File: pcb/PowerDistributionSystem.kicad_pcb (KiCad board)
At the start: 4 copper layers, 60 x 59 mm, 92 parts, among them J1 Pin-Out, J2 JST-PH, J3 JST-PH, J4 JST-PH, J5 JST-PH, J6 JST-PH, U1 D24V7F5, U2 D24V7F3, U3 TMC2209-LA-T, U4 TMC2209-LA-T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

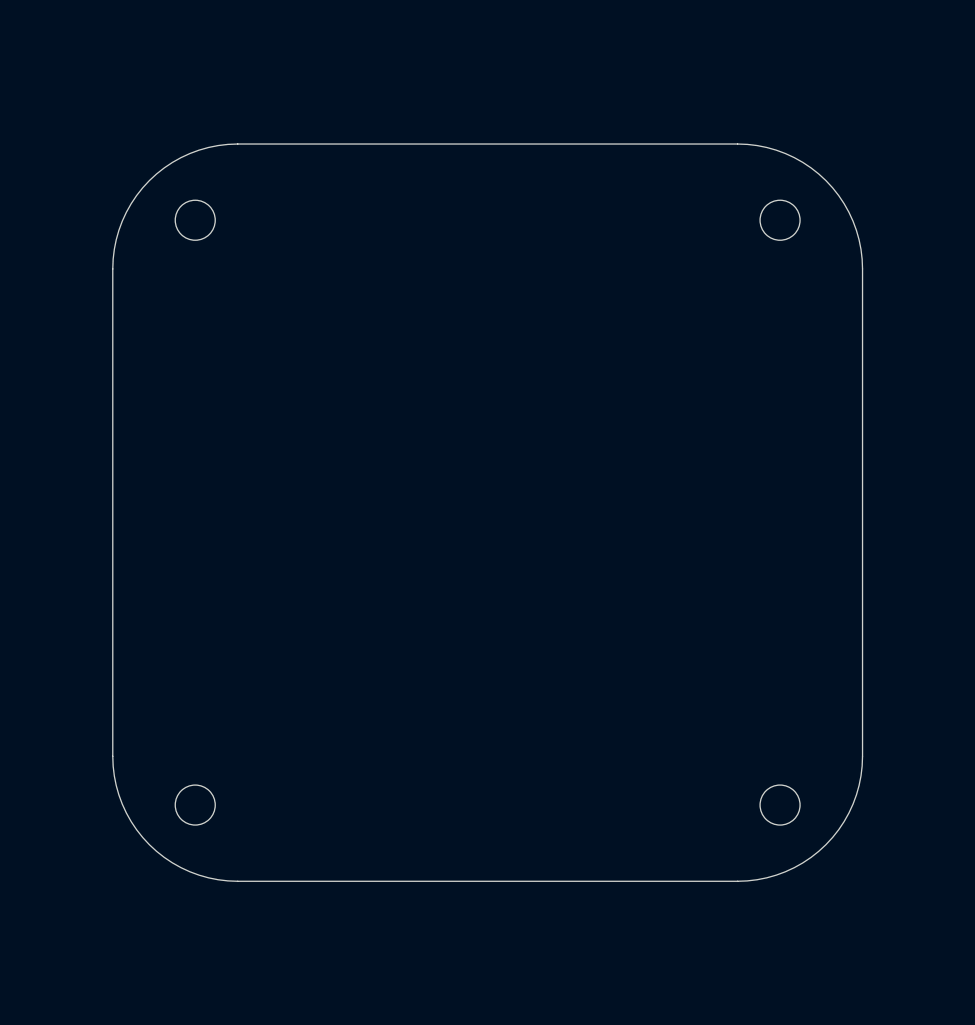
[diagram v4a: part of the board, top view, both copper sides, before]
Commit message: Using same layout as the main stack.
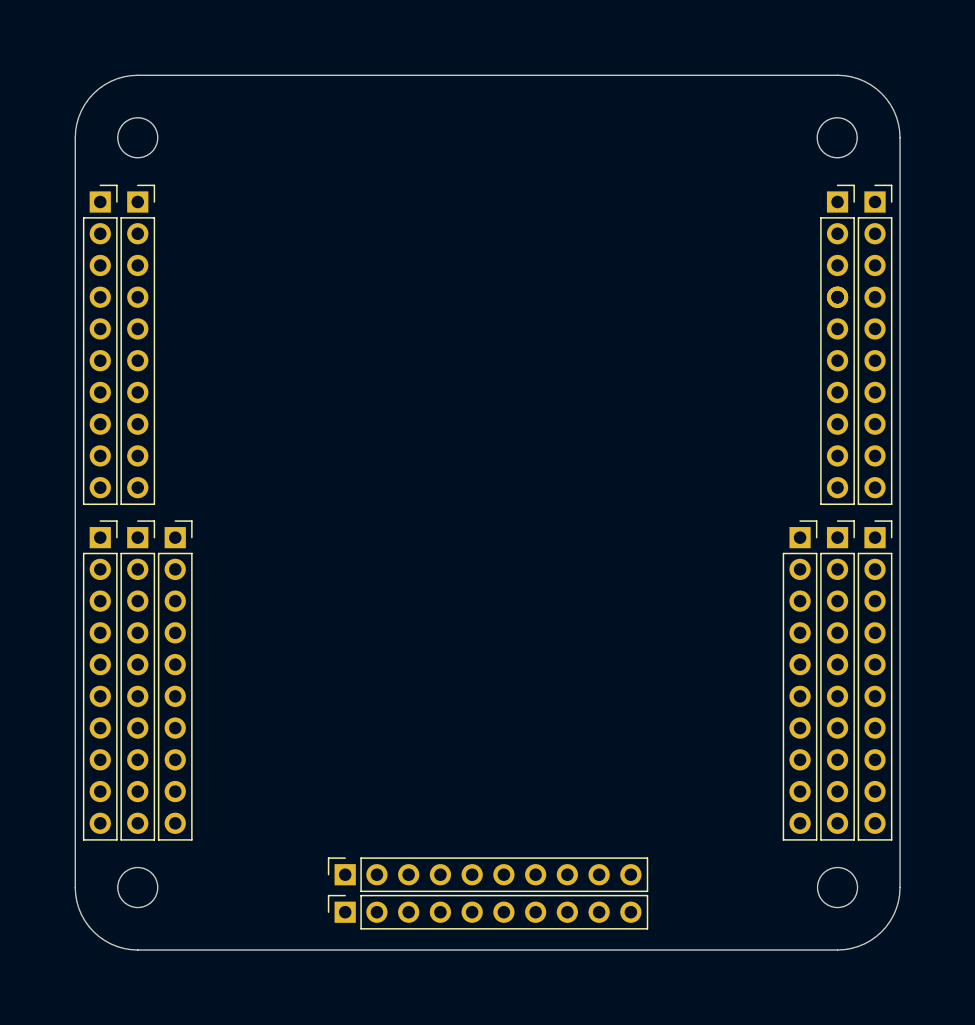
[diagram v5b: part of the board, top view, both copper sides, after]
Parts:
- removed H17, H18, H19, H20: MountingHole, MountingHole:MountingHole_3.2mm_M3
- added ?: , , F.Cu at (178.0, 82.8)
- added H1: M3, MountingHole:MountingHole_3.2mm_M3, F.Cu at (122.0, 130.0)
- added H2: M3, MountingHole:MountingHole_3.2mm_M3, F.Cu at (178.0, 70.0)
- added H3: M3, MountingHole:MountingHole_3.2mm_M3, F.Cu at (122.0, 70.0)
- added H4: M3, MountingHole:MountingHole_3.2mm_M3, F.Cu at (178.0, 130.0)
- added J11: Conn_01x10, pcb:Stack_Connector_1x10, F.Cu at (122.0, 75.1)
- added J12: Conn_01x10, pcb:Stack_Connector_1x10, F.Cu at (119.0, 102.0)
- added J13: Conn_01x10, pcb:Stack_Connector_1x10, F.Cu at (122.0, 102.0)
- added J14: Conn_01x10, pcb:Stack_Connector_1x10, F.Cu at (178.0, 75.1)
- added J15: Conn_01x10, pcb:Stack_Connector_1x10, F.Cu at (181.0, 75.1)
- added J16: Conn_01x10, pcb:Stack_Connector_1x10, F.Cu at (178.0, 102.0)
- added J17: Conn_01x10, pcb:Stack_Connector_1x10, F.Cu at (181.0, 102.0)
- added J18: Conn_01x10, pcb:Stack_Connector_1x10, F.Cu at (138.6, 129.0)
- added J19: Conn_01x10, pcb:Stack_Connector_1x10, F.Cu at (175.0, 102.0)
- added J21: Conn_01x10, pcb:Stack_Connector_1x10, F.Cu at (138.6, 132.0)
- added J23: Conn_01x10, pcb:Stack_Connector_1x10, F.Cu at (125.0, 102.0)
- added J3: Conn_01x10, pcb:Stack_Connector_1x10, F.Cu at (119.0, 75.1)
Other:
- board size 60 x 59 mm -> 66 x 70 mm

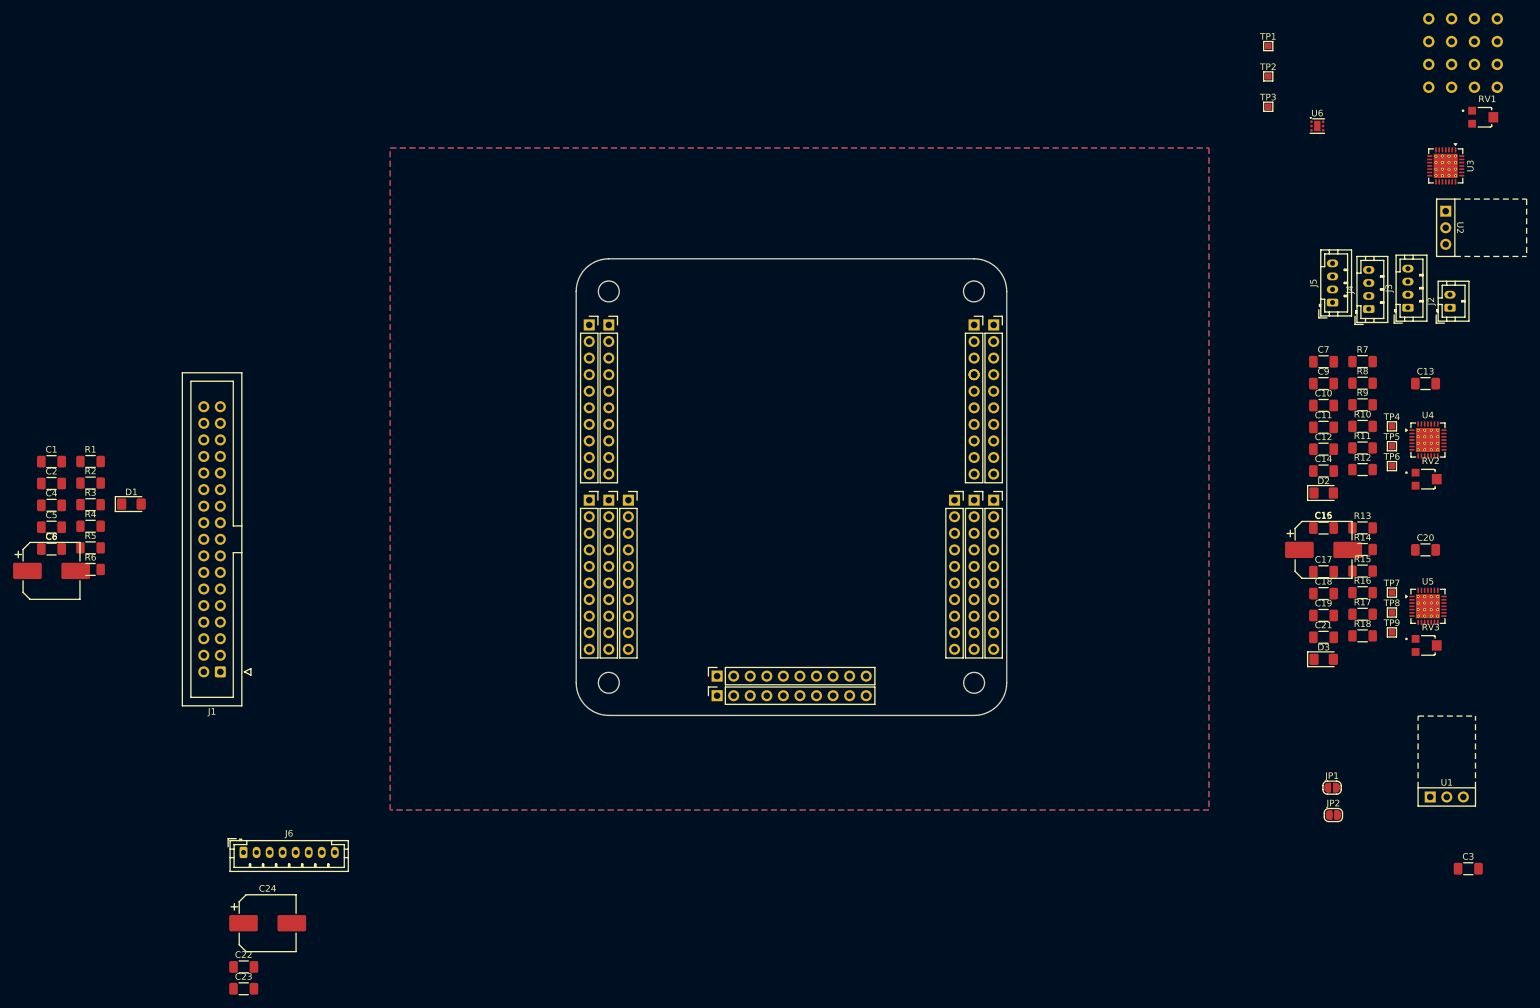
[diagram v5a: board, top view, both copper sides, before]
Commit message: Power distribution board using the PCB stack-up symbol.
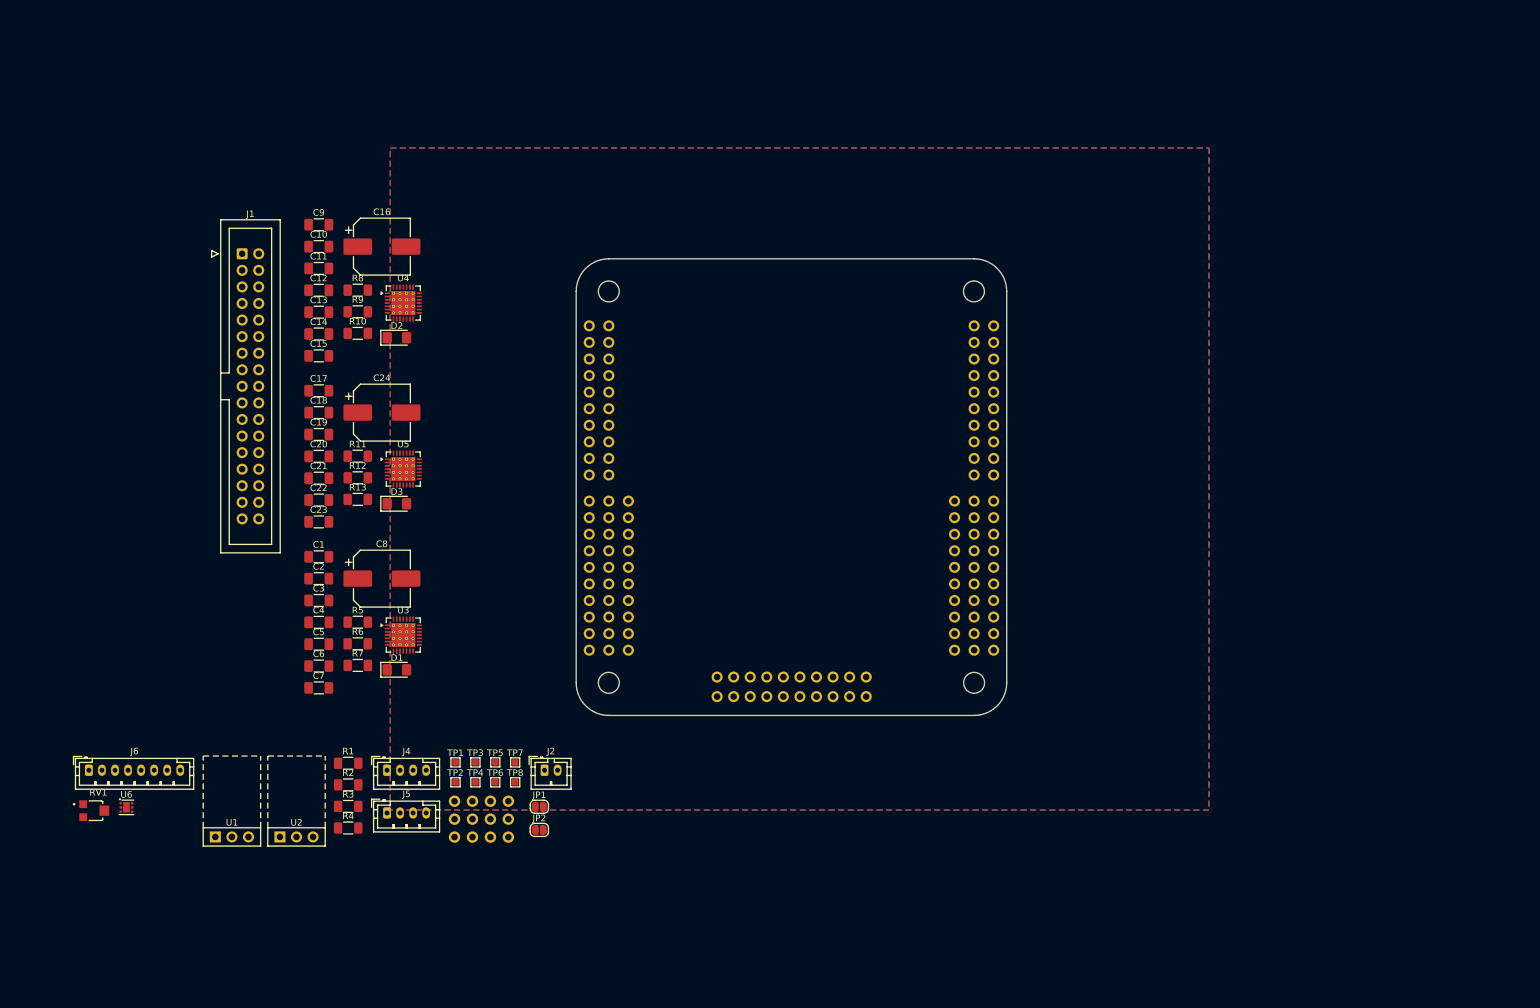
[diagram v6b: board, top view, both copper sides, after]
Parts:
- removed ?: , 
- removed H1, H2, H3, H4: M3, MountingHole:MountingHole_3.2mm_M3
- removed H1, H2, H3, H4: MountingHole_Pad_MP, pcb:Matrix_Hole
- removed J11, J12, J13, J14, J15, J16, J17, J18, J19, J21, J23, J3: Conn_01x10, pcb:Stack_Connector_1x10
- removed J3: JST-PH, Connector_JST:JST_PH_B4B-PH-K_1x04_P2.00mm_Vertical
- removed R14: 20k, Resistor_SMD:R_1206_3216Metric_Pad1.30x1.75mm_HandSolder
- removed R15: 1k, Resistor_SMD:R_1206_3216Metric_Pad1.30x1.75mm_HandSolder
- removed R16, R17: RL1206FR-070R05L, Resistor_SMD:R_1206_3216Metric_Pad1.30x1.75mm_HandSolder
- removed R18: 33k, Resistor_SMD:R_1206_3216Metric_Pad1.30x1.75mm_HandSolder
- removed RV2, RV3: 10k, pcb:TRIM_35WR10KLFTR
- removed TP9: TestPoint, TestPoint:TestPoint_Pad_1.0x1.0mm
- added C25: ~, pcb:StackConnector, F.Cu at (150.0, 100.0)
- moved RV1 238.0 mm to (43.0, 149.6)
- moved U6 210.3 mm to (48.0, 149.1)
- moved U2 199.4 mm to (74.1, 153.6), turned to 0 degrees
- moved H13 198.9 mm to (103.8, 153.7)
- moved H9 196.6 mm to (101.1, 150.9)
- moved H10 196.1 mm to (101.1, 153.7)
- moved H5 194.3 mm to (98.3, 148.2)
- moved H6 193.8 mm to (98.3, 150.9)
- moved H7 193.4 mm to (98.3, 153.7)
- moved H14 191.2 mm to (106.6, 148.2)
- moved H15 190.7 mm to (106.6, 150.9)
- moved H16 190.3 mm to (106.6, 153.7)
- moved H11 188.5 mm to (103.8, 148.2)
- moved H12 188.0 mm to (103.8, 150.9)
- moved U1 186.3 mm to (64.2, 153.6)
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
